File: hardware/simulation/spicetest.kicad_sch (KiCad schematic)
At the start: 14 parts, among them U1 ${SIM.PARAMS}, U2 ${SIM.PARAMS}

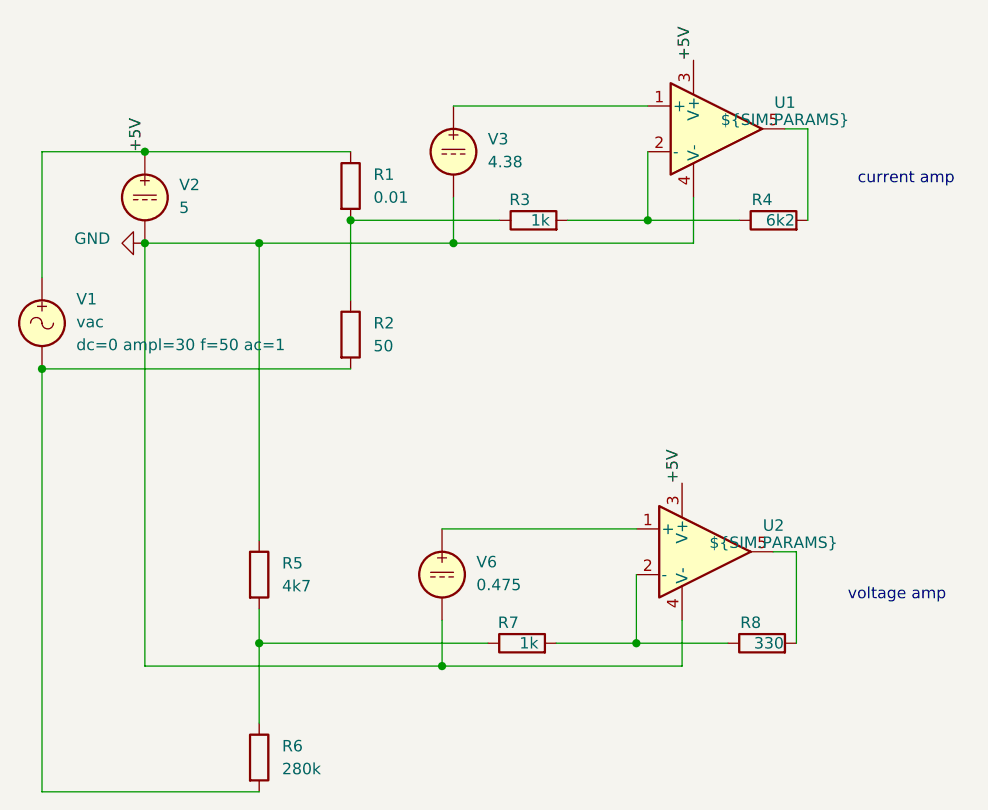
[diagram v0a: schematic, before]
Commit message: added testpoints. adjusted opamps for correct measurement. replaced hard resistors with potentiometer trimmers if necessary
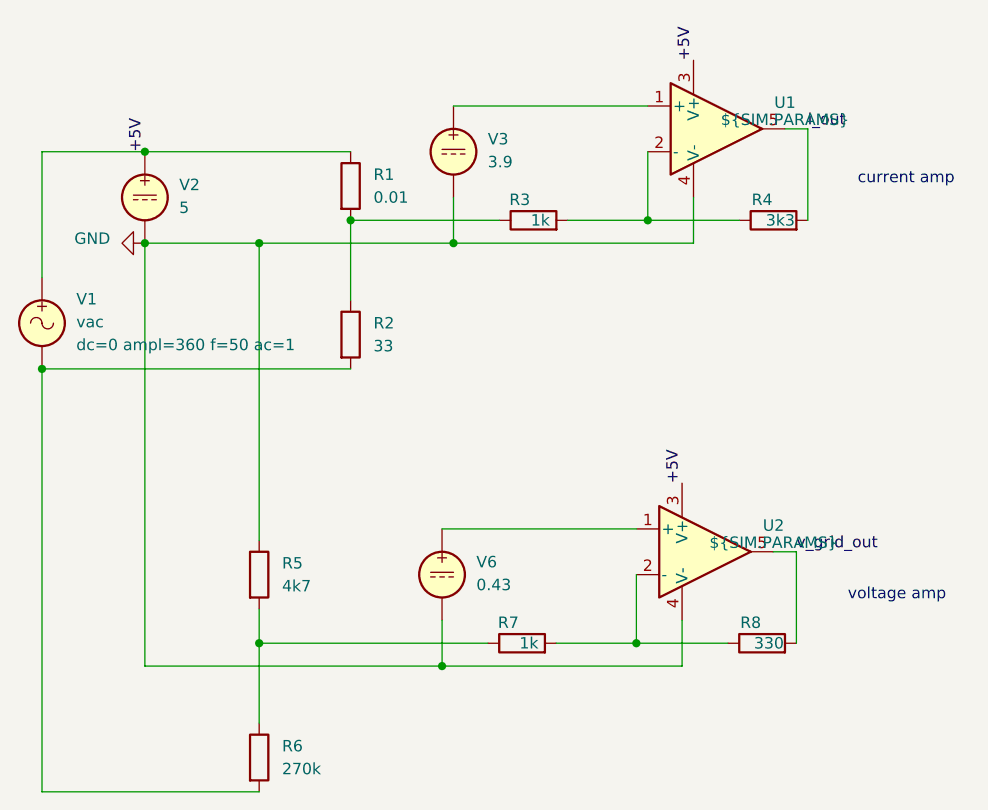
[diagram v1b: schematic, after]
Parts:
- R2: value 50 -> 33
- R4: value 6k2 -> 3k3
- R6: value 280k -> 270k
- V3: value 4.38 -> 3.9
- V6: value 0.475 -> 0.43
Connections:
- net v_grid_out: now reaches R8.2, U2.5
- net i_out: now reaches R4.2, U1.5
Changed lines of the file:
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@@
 		)
 	)
-	(label "+5V"
-		(at 110.49 59.69 90)
+	(label "v_grid_out"
+		(at 121.92 114.3 0)
 		(fields_autoplaced yes)
 		(effects
@@
 		)
 	)
+	(label "+5V"
+		(at 110.49 59.69 90)
+		(fields_autoplaced yes)
+		(effects
+			(font
+				(size 1.27 1.27)
+			)
+			(justify left bottom)
+		)
+	)
+	(label "i_out"
+		(at 123.19 67.31 0)
+		(fields_autoplaced yes)
+		(effects
+			(font
+				(size 1.27 1.27)
+			)
+			(justify left bottom)
+		)
+	)
 	(symbol
 		(lib_id "Simulation_SPICE:VSIN")
@@
 			)
 		)
-		(property "Sim.Params" "dc=0 ampl=30 f=50 ac=1"
+		(property "Sim.Params" "dc=0 ampl=360 f=50 ac=1"
 			(at 41.91 91.3101 0)
 			(effects
@@
 			)
 		)
-		(property "Value" "6k2"
+		(property "Value" "3k3"
 			(at 120.142 77.47 90)
 			(effects
@@
 			)
 		)
-		(property "Value" "4.38"
+		(property "Value" "3.9"
 			(at 87.63 70.9901 0)
 			(effects
@@
 			)
 		)
-		(property "Value" "0.475"
+		(property "Value" "0.43"
 			(at 86.36 117.9801 0)
 			(effects
@@
 			)
 		)
-		(property "Value" "50"
+		(property "Value" "33"
 			(at 74.93 91.4399 0)
 			(effects
@@
 			)
 		)
-		(property "Value" "280k"
+		(property "Value" "270k"
 			(at 64.77 138.4299 0)
 			(effects
